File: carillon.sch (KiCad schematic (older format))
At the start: 25 parts, among them P1 CONN_2, Q1 J112G, SW1 sonnette, U1 LM7805, U2 LM7812, U3 PIC10F202, U4 LM386-N3

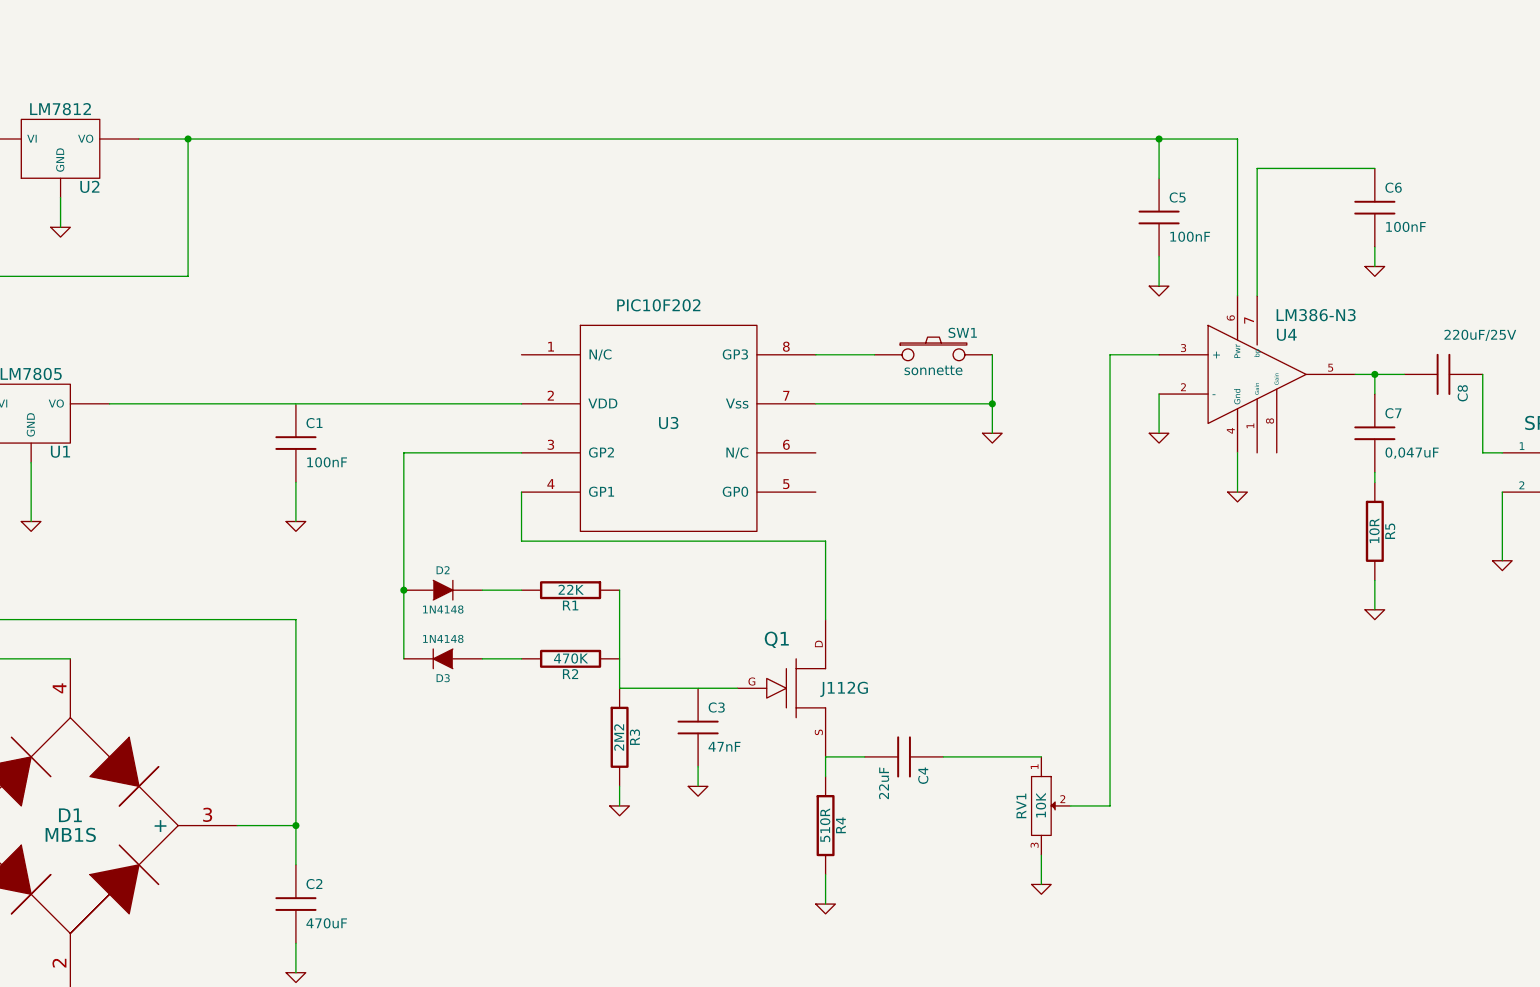
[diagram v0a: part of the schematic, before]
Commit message: ajout fichier png schéma.
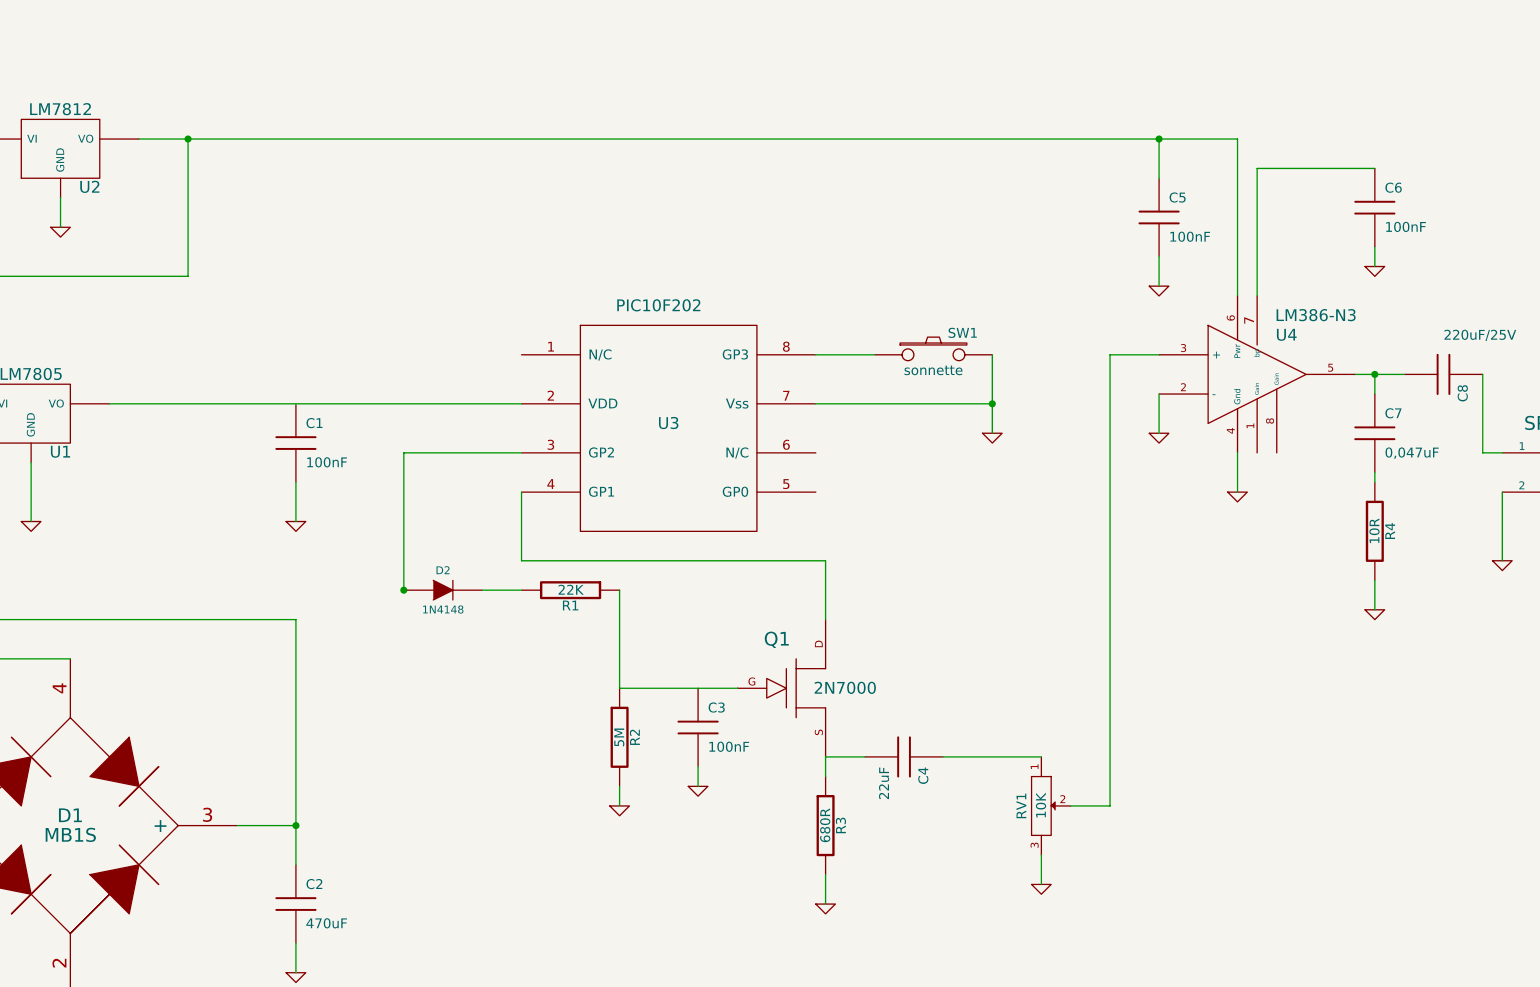
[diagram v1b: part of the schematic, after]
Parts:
- removed D3: 1N4148, symbol DIODE
- removed R2: 470K, symbol R
- C3: value 47nF -> 100nF
- Q1: value J112G -> 2N7000
- R2: renamed from R3; value 2M2 -> 5M
- R3: renamed from R4; value 510R -> 680R
- renumbered R5 to R4
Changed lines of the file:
@@
-EESchema Schematic File Version 2  date 2013-03-21 11:08:58
+EESchema Schematic File Version 2  date 2013-03-22 22:48:29
 LIBS:power
 LIBS:device
@@
 LIBS:contrib
 LIBS:valves
-EELAYER 43  0
+LIBS:carillon-cache
+EELAYER 27 0
 EELAYER END
-$Descr A4 11700 8267
+$Descr A4 11693 8268
+encoding utf-8
 Sheet 1 1
 Title ""
-Date "21 mar 2013"
+Date "23 mar 2013"
 Rev ""
 Comp ""
@@
 Wire Wire Line
 	5000 3250 4400 3250
-Wire Wire Line
-	4400 3250 4400 4300
 Connection ~ 4400 3950
 Wire Wire Line
-	4800 4300 5000 4300
-Wire Wire Line
 	5500 4950 5500 5050
-Wire Wire Line
-	6550 4100 6550 3700
-Wire Wire Line
-	6550 3700 5000 3700
-Wire Wire Line
-	5000 3700 5000 3450
 Wire Wire Line
 	6550 5400 6550 5550
@@
 	3850 3400 3850 3600
 Wire Wire Line
-	8650 2450 8650 1650
-Wire Wire Line
-	8650 1650 3050 1650
+	8650 1650 8650 2450
+Wire Wire Line
+	3050 1650 8650 1650
 Connection ~ 3300 1650
 Wire Wire Line
@@
 F 0 "#PWR11" H 8250 2400 30  0001 C CNN
 F 1 "GND" H 8250 2330 30  0001 C CNN
+F 2 "" H 8250 2400 60  0001 C CNN
+F 3 "" H 8250 2400 60  0001 C CNN
 	1    8250 2400
 	1    0    0    -1
@@
 F 0 "C5" H 8300 2150 50  0000 L CNN
 F 1 "100nF" H 8300 1950 50  0000 L CNN
+F 2 "" H 8250 2050 60  0001 C CNN
+F 3 "" H 8250 2050 60  0001 C CNN
 	1    8250 2050
 	1    0    0    -1
@@
 F 0 "P1" V 1100 5150 40  0000 C CNN
 F 1 "CONN_2" V 1200 5150 40  0000 C CNN
+F 2 "" H 1150 5150 60  0001 C CNN
+F 3 "" H 1150 5150 60  0001 C CNN
 	1    1150 5150
 	-1   0    0    1
@@
 F 0 "#PWR1" H 1850 5400 30  0001 C CNN
 F 1 "GND" H 1850 5330 30  0001 C CNN
+F 2 "" H 1850 5400 60  0001 C CNN
+F 3 "" H 1850 5400 60  0001 C CNN
 	1    1850 5400
 	1    0    0    -1
@@
 F 0 "#PWR5" H 3850 5900 30  0001 C CNN
 F 1 "GND" H 3850 5830 30  0001 C CNN
+F 2 "" H 3850 5900 60  0001 C CNN
+F 3 "" H 3850 5900 60  0001 C CNN
 	1    3850 5900
 	1    0    0    -1
@@
 F 0 "C2" H 3900 5650 50  0000 L CNN
 F 1 "470uF" H 3900 5450 50  0000 L CNN
+F 2 "" H 3850 5550 60  0001 C CNN
+F 3 "" H 3850 5550 60  0001 C CNN
 	1    3850 5550
 	1    0    0    -1
@@
 F 0 "D1" H 2700 5200 70  0000 C CNN
 F 1 "MB1S" H 2700 5100 70  0000 C CNN
+F 2 "" H 2700 5150 60  0001 C CNN
+F 3 "" H 2700 5150 60  0001 C CNN
 	1    2700 5150
 	1    0    0    -1
@@
 F 0 "U3" H 5750 900 60  0000 C CNN
 F 1 "PIC10F202" H 5700 1500 60  0000 C CNN
+F 2 "" H 4900 2000 60  0001 C CNN
+F 3 "" H 4900 2000 60  0001 C CNN
 	1    4900 2000
 	1    0    0    -1
@@
 F 0 "U1" H 2650 2854 60  0000 C CNN
 F 1 "LM7805" H 2500 3250 60  0000 C CNN
+F 2 "" H 2500 3050 60  0001 C CNN
+F 3 "" H 2500 3050 60  0001 C CNN
 	1    2500 3050
 	1    0    0    -1
@@
 F 0 "#PWR14" H 9350 2300 30  0001 C CNN
 F 1 "GND" H 9350 2230 30  0001 C CNN
+F 2 "" H 9350 2300 60  0001 C CNN
+F 3 "" H 9350 2300 60  0001 C CNN
 	1    9350 2300
 	1    0    0    -1
@@
 F 0 "C6" H 9400 2100 50  0000 L CNN
 F 1 "100nF" H 9400 1900 50  0000 L CNN
+F 2 "" H 9350 2000 60  0001 C CNN
+F 3 "" H 9350 2000 60  0001 C CNN
 	1    9350 2000
 	1    0    0    -1
@@
 F 0 "#PWR3" H 2650 2100 30  0001 C CNN
 F 1 "GND" H 2650 2030 30  0001 C CNN
+F 2 "" H 2650 2100 60  0001 C CNN
+F 3 "" H 2650 2100 60  0001 C CNN
 	1    2650 2100
 	1    0    0    -1
@@
 F 0 "#PWR12" H 8250 3150 30  0001 C CNN
 F 1 "GND" H 8250 3080 30  0001 C CNN
+F 2 "" H 8250 3150 60  0001 C CNN
+F 3 "" H 8250 3150 60  0001 C CNN
 	1    8250 3150
 	1    0    0    -1
@@
 F 0 "#PWR13" H 8650 3450 30  0001 C CNN
 F 1 "GND" H 8650 3380 30  0001 C CNN
+F 2 "" H 8650 3450 60  0001 C CNN
+F 3 "" H 8650 3450 60  0001 C CNN
 	1    8650 3450
 	1    0    0    -1
@@
 F 0 "#PWR8" H 6550 5550 30  0001 C CNN
 F 1 "GND" H 6550 5480 30  0001 C CNN
+F 2 "" H 6550 5550 60  0001 C CNN
+F 3 "" H 6550 5550 60  0001 C CNN
 	1    6550 5550
 	1    0    0    -1
 $EndComp
 $Comp
-L R R4
+L R R3
 U 1 1 514B1A00
 P 6550 5150
-F 0 "R4" V 6630 5150 50  0000 C CNN
-F 1 "510R" V 6550 5150 50  0000 C CNN
+F 0 "R3" V 6630 5150 50  0000 C CNN
+F 1 "680R" V 6550 5150 50  0000 C CNN
+F 2 "" H 6550 5150 60  0001 C CNN
+F 3 "" H 6550 5150 60  0001 C CNN
 	1    6550 5150
 	1    0    0    -1
@@
 F 0 "#PWR6" H 5500 5050 30  0001 C CNN
 F 1 "GND" H 5500 4980 30  0001 C CNN
+F 2 "" H 5500 5050 60  0001 C CNN
+F 3 "" H 5500 5050 60  0001 C CNN
 	1    5500 5050
 	1    0    0    -1
@@
 F 0 "#PWR7" H 5900 4950 30  0001 C CNN
 F 1 "GND" H 5900 4880 30  0001 C CNN
+F 2 "" H 5900 4950 60  0001 C CNN
+F 3 "" H 5900 4950 60  0001 C CNN
 	1    5900 4950
 	1    0    0    -1
-$EndComp
-$Comp
-L R R2
-U 1 1 514B197D
-P 5250 4300
-F 0 "R2" V 5330 4300 50  0000 C CNN
-F 1 "470K" V 5250 4300 50  0000 C CNN
-	1    5250 4300
-	0    1    1    0
-$EndComp
-$Comp
-L DIODE D3
-U 1 1 514B196A
-P 4600 4300
-F 0 "D3" H 4600 4400 40  0000 C CNN
-F 1 "1N4148" H 4600 4200 40  0000 C CNN
-	1    4600 4300
-	-1   0    0    1
 $EndComp
 $Comp
@@
 F 0 "R1" V 5330 3950 50  0000 C CNN
 F 1 "22K" V 5250 3950 50  0000 C CNN
+F 2 "" H 5250 3950 60  0001 C CNN
+F 3 "" H 5250 3950 60  0001 C CNN
 	1    5250 3950
 	0    1    1    0
@@
 F 0 "D2" H 4600 4050 40  0000 C CNN
 F 1 "1N4148" H 4600 3850 40  0000 C CNN
+F 2 "" H 4600 3950 60  0001 C CNN
+F 3 "" H 4600 3950 60  0001 C CNN
 	1    4600 3950
 	1    0    0    -1
@@
 F 0 "#PWR10" H 7650 5450 30  0001 C CNN
 F 1 "GND" H 7650 5380 30  0001 C CNN
+F 2 "" H 7650 5450 60  0001 C CNN
+F 3 "" H 7650 5450 60  0001 C CNN
 	1    7650 5450
 	1    0    0    -1
@@
 F 0 "C4" H 7000 4900 50  0000 L CNN
 F 1 "22uF" H 7000 4700 50  0000 L CNN
+F 2 "" H 6950 4800 60  0001 C CNN
+F 3 "" H 6950 4800 60  0001 C CNN
 	1    6950 4800
 	0    1    1    0
@@
 F 0 "#PWR9" H 7400 3150 30  0001 C CNN
 F 1 "GND" H 7400 3080 30  0001 C CNN
+F 2 "" H 7400 3150 60  0001 C CNN
+F 3 "" H 7400 3150 60  0001 C CNN
 	1    7400 3150
 	1    0    0    -1
@@
 F 0 "#PWR16" H 10000 3800 30  0001 C CNN
 F 1 "GND" H 10000 3730 30  0001 C CNN
+F 2 "" H 10000 3800 60  0001 C CNN
+F 3 "" H 10000 3800 60  0001 C CNN
 	1    10000 3800
 	1    0    0    -1
@@
 F 0 "C8" H 9750 2950 50  0000 L CNN
 F 1 "220uF/25V" V 9500 2850 50  0000 L CNN
+F 2 "" H 9700 2850 60  0001 C CNN
+F 3 "" H 9700 2850 60  0001 C CNN
 	1    9700 2850
 	0    1    1    0
@@
 F 0 "C7" H 9400 3250 50  0000 L CNN
 F 1 "0,047uF" H 9400 3050 50  0000 L CNN
+F 2 "" H 9350 3150 60  0001 C CNN
+F 3 "" H 9350 3150 60  0001 C CNN
 	1    9350 3150
 	1    0    0    -1
 $EndComp
 $Comp
-L R R5
+L R R4
 U 1 1 514B189E
 P 9350 3650
-F 0 "R5" V 9430 3650 50  0000 C CNN
+F 0 "R4" V 9430 3650 50  0000 C CNN
 F 1 "10R" V 9350 3650 50  0000 C CNN
+F 2 "" H 9350 3650 60  0001 C CNN
+F 3 "" H 9350 3650 60  0001 C CNN
 	1    9350 3650
 	1    0    0    -1
@@
 F 0 "#PWR4" H 3850 3600 30  0001 C CNN
 F 1 "GND" H 3850 3530 30  0001 C CNN
+F 2 "" H 3850 3600 60  0001 C CNN
+F 3 "" H 3850 3600 60  0001 C CNN
 	1    3850 3600
 	1    0    0    -1
@@
 F 0 "#PWR2" H 2500 3600 30  0001 C CNN
 F 1 "GND" H 2500 3530 30  0001 C CNN
+F 2 "" H 2500 3600 60  0001 C CNN
+F 3 "" H 2500 3600 60  0001 C CNN
 	1    2500 3600
 	1    0    0    -1
@@
 F 0 "C1" H 3900 3300 50  0000 L CNN
 F 1 "100nF" H 3900 3100 50  0000 L CNN
+F 2 "" H 3850 3200 60  0001 C CNN
+F 3 "" H 3850 3200 60  0001 C CNN
 	1    3850 3200
 	1    0    0    -1
@@
 F 0 "SP1" H 10200 3600 70  0000 C CNN
 F 1 "8Ohm/0,5W" H 10600 3000 70  0000 C CNN
+F 2 "" H 10300 3350 60  0001 C CNN
+F 3 "" H 10300 3350 60  0001 C CNN
 	1    10300 3350
 	1    0    0    -1
@@
 F 0 "#PWR15" H 9350 4050 30  0001 C CNN
 F 1 "GND" H 9350 3980 30  0001 C CNN
+F 2 "" H 9350 4050 60  0001 C CNN
+F 3 "" H 9350 4050 60  0001 C CNN
 	1    9350 4050
 	1    0    0    -1
@@
 F 0 "RV1" H 7650 4950 50  0000 C CNN
 F 1 "10K" H 7650 5050 50  0000 C CNN
+F 2 "" H 7650 5050 60  0001 C CNN
+F 3 "" H 7650 5050 60  0001 C CNN
 	1    7650 5050
 	0    1    1    0
@@
 P 5900 4650
 F 0 "C3" H 5950 4750 50  0000 L CNN
-F 1 "47nF" H 5950 4550 50  0000 L CNN
+F 1 "100nF" H 5950 4550 50  0000 L CNN
+F 2 "" H 5900 4650 60  0001 C CNN
+F 3 "" H 5900 4650 60  0001 C CNN
 	1    5900 4650
 	1    0    0    -1
 $EndComp
 $Comp
-L R R3
+L R R2
 U 1 1 514B17E2
 P 5500 4700
-F 0 "R3" V 5580 4700 50  0000 C CNN
-F 1 "2M2" V 5500 4700 50  0000 C CNN
+F 0 "R2" V 5580 4700 50  0000 C CNN
+F 1 "5M" V 5500 4700 50  0000 C CNN
+F 2 "" H 5500 4700 60  0001 C CNN
+F 3 "" H 5500 4700 60  0001 C CNN
 	1    5500 4700
 	1    0    0    -1
@@
 F 0 "SW1" H 7250 2860 50  0000 C CNN
 F 1 "sonnette" H 7100 2670 50  0000 C CNN
+F 2 "" H 7100 2750 60  0001 C CNN
+F 3 "" H 7100 2750 60  0001 C CNN
 	1    7100 2750
 	1    0    0    -1
@@
 F 0 "U2" H 2800 1504 60  0000 C CNN
 F 1 "LM7812" H 2650 1900 60  0000 C CNN
+F 2 "" H 2650 1700 60  0001 C CNN
+F 3 "" H 2650 1700 60  0001 C CNN
 	1    2650 1700
 	1    0    0    -1
@@
 F 0 "U4" H 8900 3050 60  0000 C CNN
 F 1 "LM386-N3" H 9050 3150 60  0000 C CNN
+F 2 "" H 8750 2850 60  0001 C CNN
+F 3 "" H 8750 2850 60  0001 C CNN
 	1    8750 2850
 	1    0    0    -1
@@
 P 6400 4450
 F 0 "Q1" H 6303 4700 70  0000 C CNN
-F 1 "J112G" H 6650 4450 60  0000 C CNN
+F 1 "2N7000" H 6650 4450 60  0000 C CNN
+F 2 "" H 6400 4450 60  0001 C CNN
+F 3 "" H 6400 4450 60  0001 C CNN
 	1    6400 4450
 	1    0    0    -1
 $EndComp
+Wire Wire Line
+	5000 3450 5000 3800
+Wire Wire Line
+	5000 3800 6550 3800
+Wire Wire Line
+	6550 3800 6550 4100
+Wire Wire Line
+	4400 3250 4400 3950
 $EndSCHEMATC

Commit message: mise à jour schéma
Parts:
- C3: value 100nF -> 150nF
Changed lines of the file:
@@
-EESchema Schematic File Version 2  date 2013-03-22 22:48:29
+EESchema Schematic File Version 2  date 2013-03-23 08:24:05
 LIBS:power
 LIBS:device
@@
 P 5900 4650
 F 0 "C3" H 5950 4750 50  0000 L CNN
-F 1 "100nF" H 5950 4550 50  0000 L CNN
+F 1 "150nF" H 5950 4550 50  0000 L CNN
 F 2 "" H 5900 4650 60  0001 C CNN
 F 3 "" H 5900 4650 60  0001 C CNN
